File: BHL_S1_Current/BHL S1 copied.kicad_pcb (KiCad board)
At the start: 2 copper layers, 82 x 82 mm, 96 parts, among them J1 Conn_01x03_Pin, J2 Conn_01x03_Pin, Q1 CSD19502Q5B, Q2 CSD19502Q5B, Q3 CSD19502Q5B, Q4 CSD19502Q5B, Q5 CSD19502Q5B, Q6 CSD19502Q5B, SW1 SW_Push, U1 ME6211C30M5, U2 SPX3819M5-L-5-0, U3 Solder Pad, U4 STM32G431CBUx, Y2 8MHz

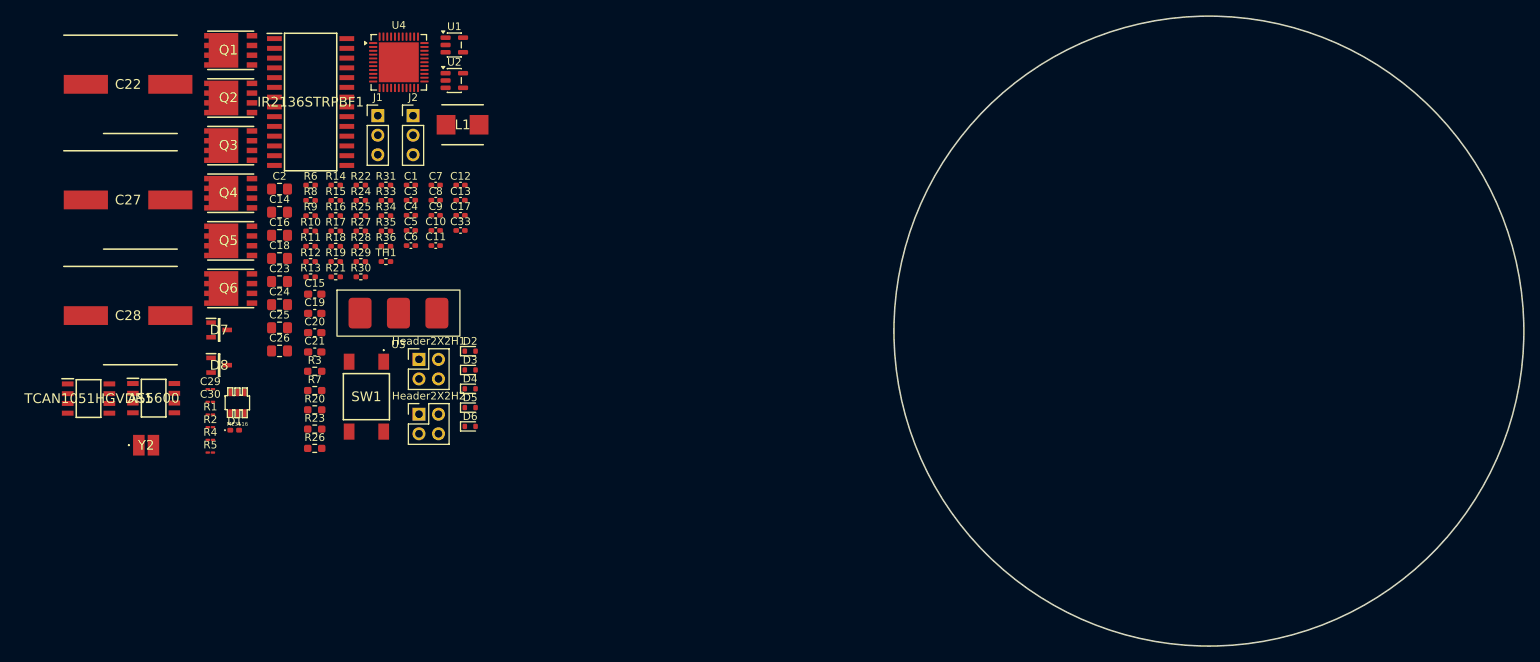
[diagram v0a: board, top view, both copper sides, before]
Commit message: Cleanup, Organization, and some edits
Editing the schematic and the PCB. Fixed a lot of ERC errors. Organized the mess that it originally was.
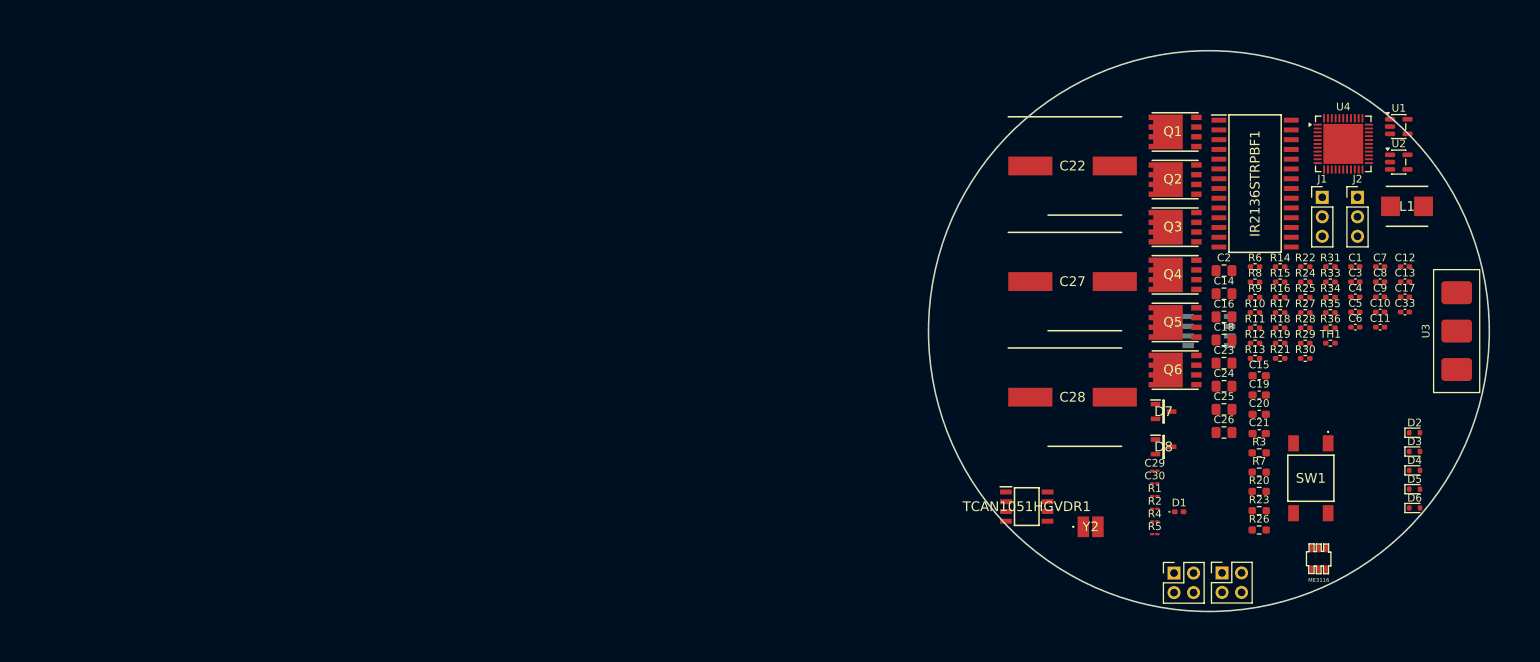
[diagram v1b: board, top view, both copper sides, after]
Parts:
- AS5600: moved to B.Cu
- moved ME3116 142.2 mm to (175.8, 128.7)
- moved U3 137.8 mm to (193.8, 99.0), turned to 90 degrees
- moved AS5600 137.6 mm to (161.5, 99.0), turned to 180 degrees
- moved C12 123.4 mm to (187.0, 90.6)
- moved C13 123.4 mm to (187.0, 92.6)
- moved C17 123.4 mm to (187.0, 94.5)
- moved C29 123.4 mm to (154.5, 117.2)
- moved C30 123.4 mm to (154.5, 118.8)
- moved C33 123.4 mm to (187.0, 96.5)
- moved D2 123.4 mm to (188.3, 112.2)
- moved D3 123.4 mm to (188.3, 114.7)
- moved D4 123.4 mm to (188.3, 117.1)
- moved D5 123.4 mm to (188.3, 119.6)
- moved D6 123.4 mm to (188.3, 122.0)
- moved R1 123.4 mm to (154.5, 120.5)
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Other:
- board size 82 x 82 mm -> 73 x 73 mm

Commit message: saved pcb
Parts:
- U4: footprint Package_DFN_QFN:QFN-44-1EP_7x7mm_P0.5mm_EP5.2x5.2mm -> Footprint for BHL S1:STM32G431CBU6_MCU
- moved U4 0.38 mm to (179.1, 74.2)
